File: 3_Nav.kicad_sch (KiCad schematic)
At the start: 36 parts, among them J401 GNSS, Q401 Q_NMOS, SW401 SW_Push, SW402 SW_Push, U401 STM32F446VETx, Y401 YXC YSX321SL

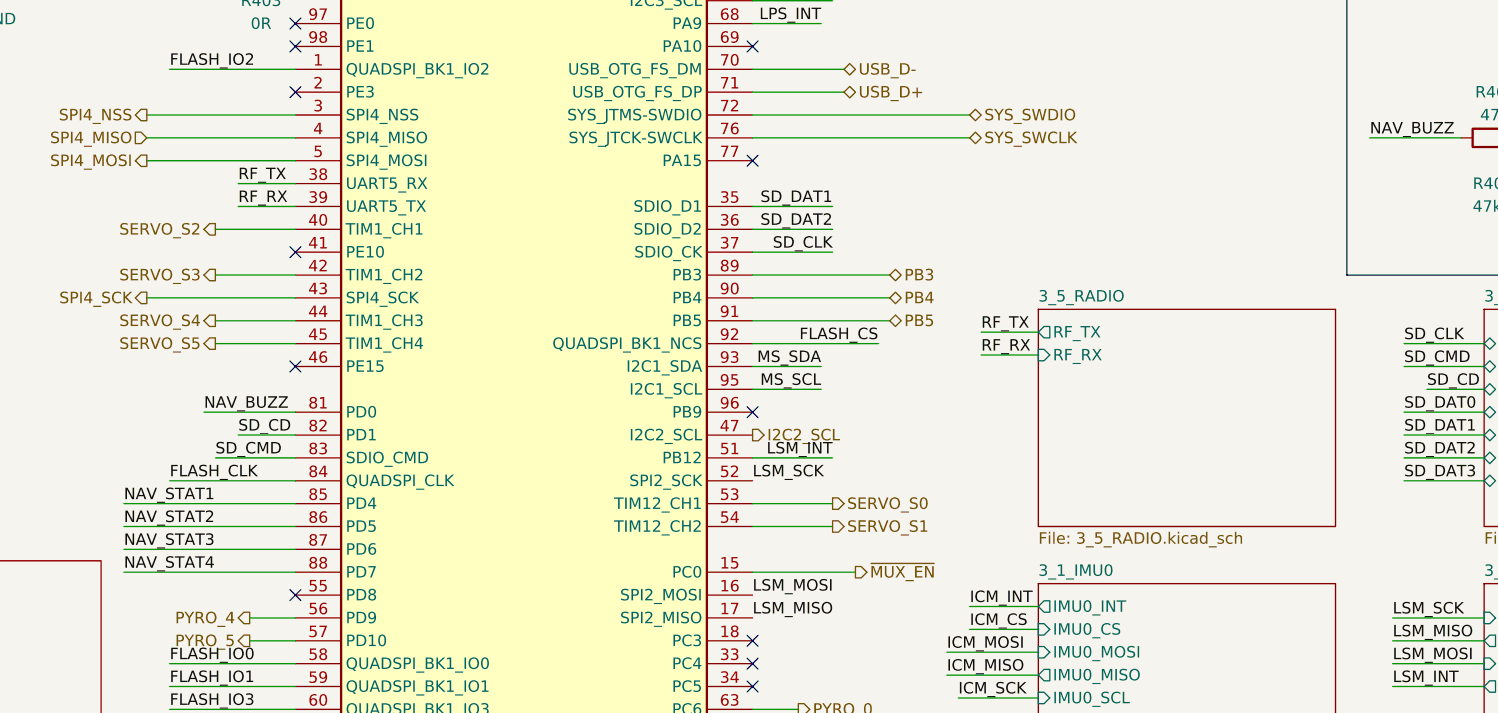
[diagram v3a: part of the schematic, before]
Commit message: Changed the board to support any telemetry radio
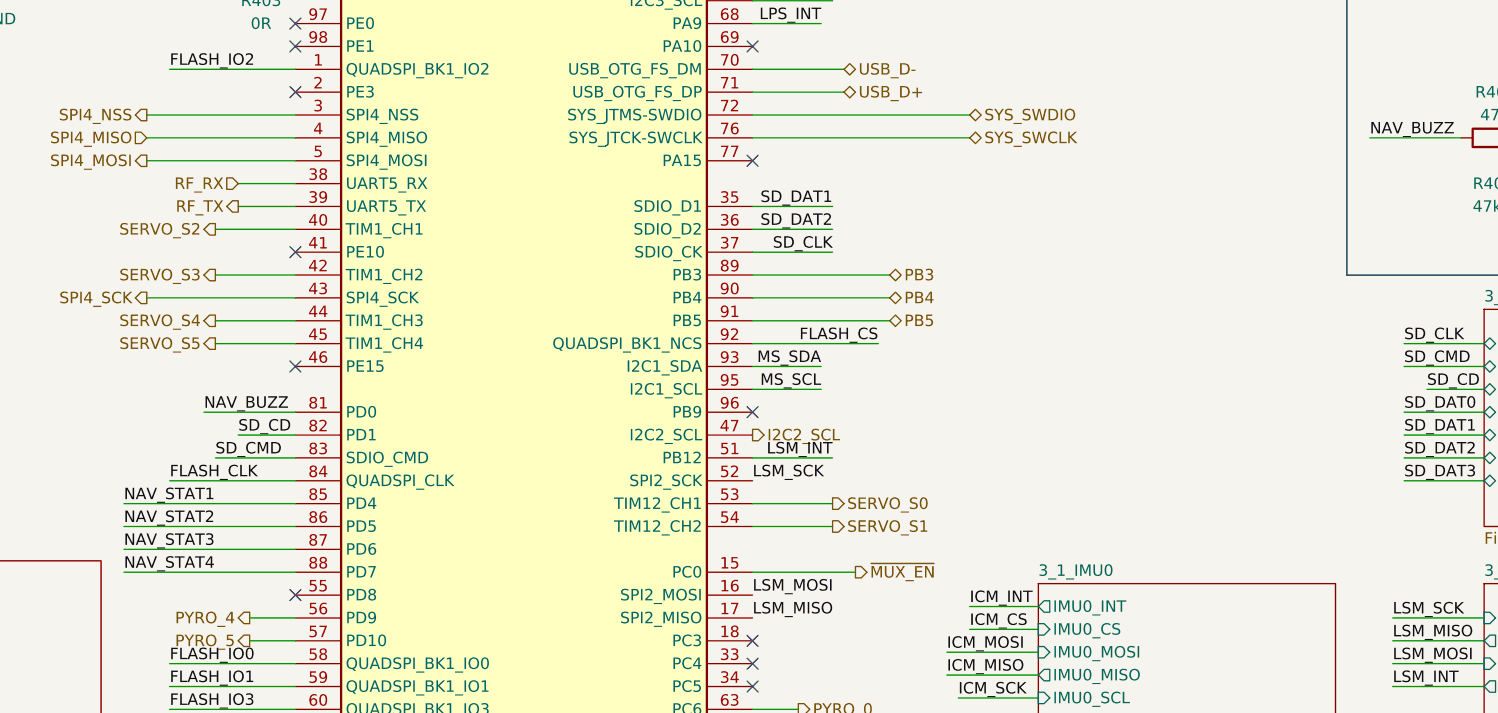
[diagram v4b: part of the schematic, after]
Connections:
- net RF_RX: now also U401.38 (PE7); no longer U401.39 (PE8)
- net RF_TX: now also U401.39 (PE8); no longer U401.38 (PE7)
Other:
- removed sheet 3_5_RADIO
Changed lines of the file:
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@@
 	(wire
 		(pts
-			(xy 190.5 110.49) (xy 196.85 110.49)
-		)
-		(stroke
-			(width 0)
-			(type default)
-		)
-	)
-	(wire
-		(pts
 			(xy 31.75 182.88) (xy 39.37 182.88)
 		)
@@
 	(wire
 		(pts
-			(xy 190.5 113.03) (xy 196.85 113.03)
-		)
-		(stroke
-			(width 0)
-			(type default)
-		)
-	)
-	(wire
-		(pts
 			(xy 165.1 160.02) (xy 173.99 160.02)
 		)
@@
 		)
 	)
-	(label "RF_TX"
-		(at 190.5 110.49 0)
-		(effects
-			(font
-				(size 1.27 1.27)
-			)
-			(justify left bottom)
-		)
-	)
 	(label "NAV_STAT1"
 		(at 208.28 48.26 0)
@@
 		)
 	)
-	(label "RF_RX"
-		(at 190.5 113.03 0)
-		(effects
-			(font
-				(size 1.27 1.27)
-			)
-			(justify left bottom)
-		)
-	)
 	(label "GPS_RX"
 		(at 172.72 53.34 180)
@@
 		)
 	)
-	(label "RF_RX"
-		(at 107.95 96.52 0)
-		(effects
-			(font
-				(size 1.27 1.27)
-			)
-			(justify left bottom)
-		)
-	)
 	(label "ICM_CS"
 		(at 172.72 63.5 180)
@@
 		)
 	)
-	(label "RF_TX"
-		(at 107.95 93.98 0)
-		(effects
-			(font
-				(size 1.27 1.27)
-			)
-			(justify left bottom)
-		)
-	)
 	(label "FLASH_IO0"
 		(at 62.23 105.41 180)
@@
 		)
 	)
+	(hierarchical_label "RF_RX"
+		(shape input)
+		(at 107.95 93.98 180)
+		(effects
+			(font
+				(size 1.27 1.27)
+			)
+			(justify right)
+		)
+	)
 	(hierarchical_label "PB4"
 		(shape bidirectional)
@@
 		)
 	)
+	(hierarchical_label "RF_TX"
+		(shape output)
+		(at 107.95 96.52 180)
+		(effects
+			(font
+				(size 1.27 1.27)
+			)
+			(justify right)
+		)
+	)
 	(hierarchical_label "SPI4_MISO"
 		(shape input)
@@
 				)
 			)
-		)
-	)
-	(sheet
-		(at 196.85 107.95)
-		(size 33.02 24.13)
-		(exclude_from_sim no)
-		(in_bom yes)
-		(on_board yes)
-		(dnp no)
-		(fields_autoplaced yes)
-		(stroke
-			(width 0.1524)
-			(type solid)
-		)
-		(fill
-			(color 0 0 0 0)
-		)
-		(property "Sheetname" "3_5_RADIO"
-			(at 196.85 107.2384 0)
-			(show_name no)
-			(do_not_autoplace no)
-			(effects
-				(font
-					(size 1.27 1.27)
-				)
-				(justify left bottom)
-			)
-		)
-		(property "Sheetfile" "3_5_RADIO.kicad_sch"
-			(at 196.85 132.6646 0)
-			(show_name no)
-			(do_not_autoplace no)
-			(effects
-				(font
-					(size 1.27 1.27)
-				)
-				(justify left top)
-			)
-		)
-		(pin "RF_TX" output
-			(at 196.85 110.49 180)
-			(effects
-				(font
-					(size 1.27 1.27)
-				)
-				(justify left)
-			)
-		)
-		(pin "RF_RX" input
-			(at 196.85 113.03 180)
-			(effects
-				(font
-					(size 1.27 1.27)
-				)
-				(justify left)
-			)
-		)
-		(instances
-			(project "polaris"
-				(path "/cfb90e19-9fbe-47a1-a5ac-df522853d1d0/2c635aac-d26f-4bb6-b325-c281bd24fb50"
-					(page "10")
-				)
-			)
